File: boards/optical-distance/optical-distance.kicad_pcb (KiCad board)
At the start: 2 copper layers, 25 x 19.5 mm, 6 parts, among them J1 CONN_02X03, M2 MountingHole_2.2mm_M2, U1 DS9638

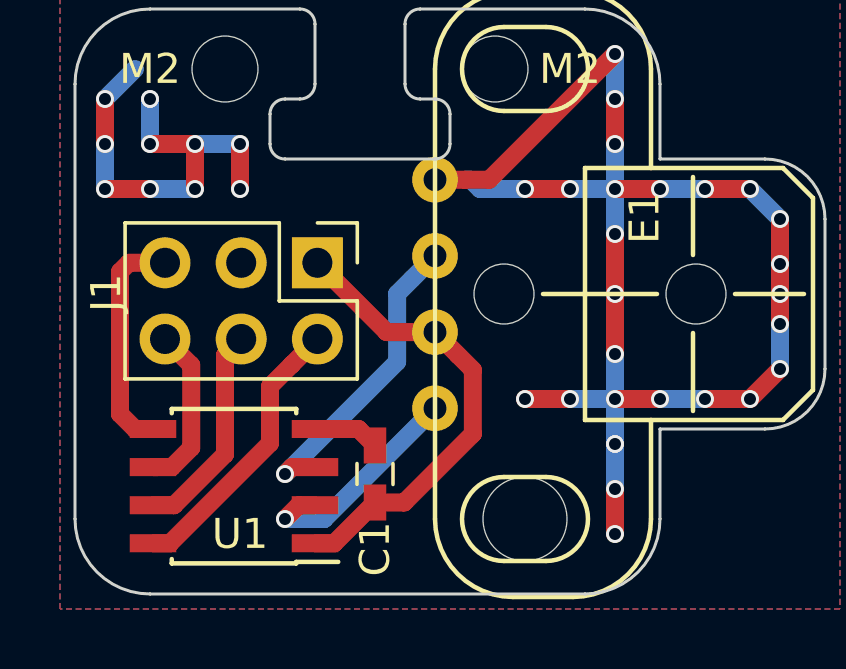
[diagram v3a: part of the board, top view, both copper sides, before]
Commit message: boards/op_v3: heat resistors in parallel added
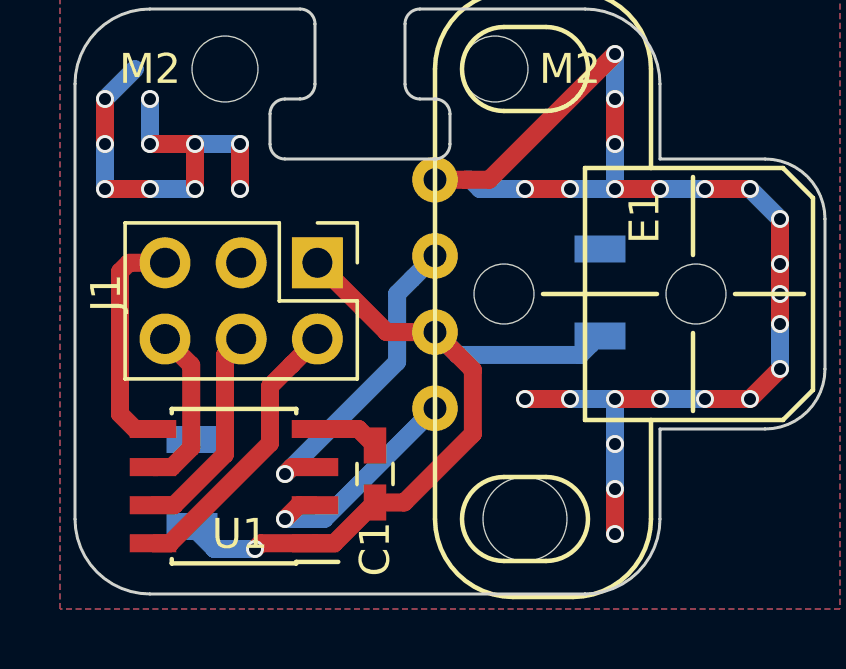
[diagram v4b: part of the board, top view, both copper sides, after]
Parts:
- added R1: HEAT, Resistors_SMD:R_1206, B.Cu at (102.5, 44.5)
- added R2: HEAT, Resistors_SMD:R_1206, B.Cu at (88.9, 50.8)
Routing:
- net /VCC: track 15.6 -> 26.1 mm, vias 0 -> 1
- net /GND: track 51.9 -> 44.9 mm, vias 26 -> 23
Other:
- board text added: "optical- distance"
- board text removed: "optical-dis- tance board"
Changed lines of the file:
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@@
-(kicad_pcb (version 4) (host pcbnew 4.0.6)
+(kicad_pcb (version 4) (host pcbnew 4.0.7-e2-6376~58~ubuntu16.04.1)
   (general
-    (links 12)
+    (links 16)
     (no_connects 1)
     (area 84.949999 34.949999 110.050001 54.550001)
     (thickness 1.6)
     (drawings 40)
-    (tracks 124)
+    (tracks 126)
     (zones 0)
-    (modules 6)
+    (modules 8)
     (nets 9)
   )
@@
     (39 F.Mask user)
     (40 Dwgs.User user)
-    (41 Cmts.User user)
+    (41 Cmts.User user hide)
     (42 Eco1.User user)
     (43 Eco2.User user)
@@
     (46 B.CrtYd user)
     (47 F.CrtYd user)
-    (48 B.Fab user)
-    (49 F.Fab user)
+    (48 B.Fab user hide)
+    (49 F.Fab user hide)
   )
   (setup
@@
     (mod_text_size 1 1)
     (mod_text_width 0.15)
-    (pad_size 1.5 1.5)
-    (pad_drill 0.6)
+    (pad_size 0.9 1.7)
+    (pad_drill 0)
     (pad_to_mask_clearance 0)
     (aux_axis_origin 0 0)
@@
     (pad 1 np_thru_hole circle (at 0 0) (size 2.2 2.2) (drill 2.2) (layers *.Cu *.Mask))
   )
+  (module Resistors_SMD:R_1206 (layer B.Cu)
+    (at 102.5 44.45 90)
+    (descr "Resistor SMD 1206, reflow soldering, Vishay (see dcrcw.pdf)")
+    (tags "resistor 1206")
+    (attr smd)
+    (fp_text reference R1 (at -0.05 0 90) (layer B.SilkS)
+      (effects (font (size 1 1) (thickness 0.15)) (justify mirror))
+    )
+    (fp_text value HEAT (at 0 -1.95 90) (layer B.Fab)
+      (effects (font (size 1 1) (thickness 0.15)) (justify mirror))
+    )
+    (fp_text user %R (at 0 0 90) (layer B.Fab)
+      (effects (font (size 0.7 0.7) (thickness 0.105)) (justify mirror))
+    )
+    (fp_line (start -1.6 -0.8) (end -1.6 0.8) (layer B.Fab) (width 0.1))
+    (fp_line (start 1.6 -0.8) (end -1.6 -0.8) (layer B.Fab) (width 0.1))
+    (fp_line (start 1.6 0.8) (end 1.6 -0.8) (layer B.Fab) (width 0.1))
+    (fp_line (start -1.6 0.8) (end 1.6 0.8) (layer B.Fab) (width 0.1))
+    (fp_line (start 1 -1.07) (end -1 -1.07) (layer B.SilkS) (width 0.12))
+    (fp_line (start -1 1.07) (end 1 1.07) (layer B.SilkS) (width 0.12))
+    (fp_line (start -2.15 1.11) (end 2.15 1.11) (layer B.CrtYd) (width 0.05))
+    (fp_line (start -2.15 1.11) (end -2.15 -1.1) (layer B.CrtYd) (width 0.05))
+    (fp_line (start 2.15 -1.1) (end 2.15 1.11) (layer B.CrtYd) (width 0.05))
+    (fp_line (start 2.15 -1.1) (end -2.15 -1.1) (layer B.CrtYd) (width 0.05))
+    (pad 1 smd rect (at -1.45 0 90) (size 0.9 1.7) (layers B.Cu B.Paste B.Mask)
+      (net 3 /VCC))
+    (pad 2 smd rect (at 1.45 0 90) (size 0.9 1.7) (layers B.Cu B.Paste B.Mask)
+      (net 4 /GND) (zone_connect 2))
+    (model ${KISYS3DMOD}/Resistors_SMD.3dshapes/R_1206.wrl
+      (at (xyz 0 0 0))
+      (scale (xyz 1 1 1))
+      (rotate (xyz 0 0 0))
+    )
+  )
+  (module Resistors_SMD:R_1206 (layer B.Cu)
+    (at 88.9 50.8 90)
+    (descr "Resistor SMD 1206, reflow soldering, Vishay (see dcrcw.pdf)")
+    (tags "resistor 1206")
+    (attr smd)
+    (fp_text reference R2 (at 0 0.1 90) (layer B.SilkS)
+      (effects (font (size 1 1) (thickness 0.15)) (justify mirror))
+    )
+    (fp_text value HEAT (at 0 -1.95 90) (layer B.Fab)
+      (effects (font (size 1 1) (thickness 0.15)) (justify mirror))
+    )
+    (fp_text user %R (at 0 0 90) (layer B.Fab)
+      (effects (font (size 0.7 0.7) (thickness 0.105)) (justify mirror))
+    )
+    (fp_line (start -1.6 -0.8) (end -1.6 0.8) (layer B.Fab) (width 0.1))
+    (fp_line (start 1.6 -0.8) (end -1.6 -0.8) (layer B.Fab) (width 0.1))
+    (fp_line (start 1.6 0.8) (end 1.6 -0.8) (layer B.Fab) (width 0.1))
+    (fp_line (start -1.6 0.8) (end 1.6 0.8) (layer B.Fab) (width 0.1))
+    (fp_line (start 1 -1.07) (end -1 -1.07) (layer B.SilkS) (width 0.12))
+    (fp_line (start -1 1.07) (end 1 1.07) (layer B.SilkS) (width 0.12))
+    (fp_line (start -2.15 1.11) (end 2.15 1.11) (layer B.CrtYd) (width 0.05))
+    (fp_line (start -2.15 1.11) (end -2.15 -1.1) (layer B.CrtYd) (width 0.05))
+    (fp_line (start 2.15 -1.1) (end 2.15 1.11) (layer B.CrtYd) (width 0.05))
+    (fp_line (start 2.15 -1.1) (end -2.15 -1.1) (layer B.CrtYd) (width 0.05))
+    (pad 1 smd rect (at -1.45 0 90) (size 0.9 1.7) (layers B.Cu B.Paste B.Mask)
+      (net 3 /VCC))
+    (pad 2 smd rect (at 1.45 0 90) (size 0.9 1.7) (layers B.Cu B.Paste B.Mask)
+      (net 4 /GND) (zone_connect 2))
+    (model ${KISYS3DMOD}/Resistors_SMD.3dshapes/R_1206.wrl
+      (at (xyz 0 0 0))
+      (scale (xyz 1 1 1))
+      (rotate (xyz 0 0 0))
+    )
+  )
   (gr_text rev3 (at 100.4 39.7) (layer B.SilkS)
     (effects (font (size 1.5 1.5) (thickness 0.3)) (justify mirror))
@@
     (effects (font (size 1 1) (thickness 0.2)) (justify mirror))
   )
-  (gr_text "optical-dis-\ntance board" (at 91.325 51.435) (layer B.SilkS)
+  (gr_text "optical-\ndistance" (at 94.5 52) (layer B.SilkS)
     (effects (font (size 1 1) (thickness 0.2)) (justify mirror))
   )
@@
     (effects (font (size 1.5 1.5) (thickness 0.3)) (justify mirror))
   )
-  (gr_text A* (at 90.5 48.5 270) (layer B.SilkS)
-    (effects (font (size 1.5 1.5) (thickness 0.3)) (justify mirror))
+  (gr_text A* (at 91 48 270) (layer B.SilkS)
+    (effects (font (size 1 1) (thickness 0.15)) (justify mirror))
   )
   (gr_text A (at 93 48 270) (layer B.SilkS)
@@
   (gr_line (start 92 40) (end 97 40) (layer Edge.Cuts) (width 0.1))
   (gr_text B* (at 88 41 270) (layer B.SilkS)
-    (effects (font (size 1.5 1.5) (thickness 0.3)) (justify mirror))
+    (effects (font (size 1 1) (thickness 0.15)) (justify mirror))
   )
   (gr_text GND (at 90.5 40.5 270) (layer B.SilkS)
-    (effects (font (size 1.5 1.2) (thickness 0.3)) (justify mirror))
+    (effects (font (size 1 1) (thickness 0.15)) (justify mirror))
   )
   (gr_text 5V (at 93 41.1 270) (layer B.SilkS)
-    (effects (font (size 1.5 1.1) (thickness 0.275)) (justify mirror))
+    (effects (font (size 1 1) (thickness 0.15)) (justify mirror))
   )
   (dimension 24 (width 0.3) (layer Dwgs.User)
@@
   (segment (start 92.46 51.54) (end 92 52) (width 0.6) (layer F.Cu) (net 2))
   (via (at 92 52) (size 0.6) (drill 0.4) (layers F.Cu B.Cu) (net 2))
+  (segment (start 91 53) (end 89.65 53) (width 0.6) (layer B.Cu) (net 3))
+  (segment (start 89.65 53) (end 88.9 52.25) (width 0.6) (layer B.Cu) (net 3))
+  (segment (start 93 52.81) (end 91.19 52.81) (width 0.6) (layer F.Cu) (net 3))
+  (segment (start 91.19 52.81) (end 91 53) (width 0.6) (layer F.Cu) (net 3))
+  (via (at 91 53) (size 0.6) (drill 0.4) (layers F.Cu B.Cu) (net 3))
+  (segment (start 97.761999 46.531999) (end 101.836617 46.531999) (width 0.6) (layer B.Cu) (net 3))
+  (segment (start 101.836617 46.531999) (end 102.19999 46.168626) (width 0.6) (layer B.Cu) (net 3))
+  (segment (start 102.19999 46.168626) (end 102.484308 45.884308) (width 0.6) (layer B.Cu) (net 3))
+  (segment (start 97 45.77) (end 97.761999 46.531999) (width 0.6) (layer B.Cu) (net 3))
   (segment (start 97 45.77) (end 95.39 45.77) (width 0.6) (layer F.Cu) (net 3))
   (segment (start 95.39 45.77) (end 93.08 43.46) (width 0.6) (layer F.Cu) (net 3))
@@
   (segment (start 93 52.81) (end 93.64 52.81) (width 0.6) (layer F.Cu) (net 3))
   (segment (start 93.64 52.81) (end 95 51.45) (width 0.6) (layer F.Cu) (net 3))
-  (segment (start 103 44.5) (end 103 46.5) (width 0.6) (layer F.Cu) (net 4))
-  (segment (start 103 42.5) (end 103 44.5) (width 0.6) (layer F.Cu) (net 4))
-  (via (at 103 44.5) (size 0.6) (drill 0.4) (layers F.Cu B.Cu) (net 4))
   (segment (start 101.5 48) (end 100 48) (width 0.6) (layer F.Cu) (net 4))
   (via (at 100 48) (size 0.6) (drill 0.4) (layers F.Cu B.Cu) (net 4))
@@
   (segment (start 103 41) (end 101.5 41) (width 0.6) (layer B.Cu) (net 4))
   (via (at 101.5 41) (size 0.6) (drill 0.4) (layers F.Cu B.Cu) (net 4))
-  (segment (start 103 46.5) (end 103 48) (width 0.6) (layer B.Cu) (net 4))
-  (via (at 103 46.5) (size 0.6) (drill 0.4) (layers F.Cu B.Cu) (net 4))
-  (segment (start 103 41) (end 103 42.5) (width 0.6) (layer B.Cu) (net 4))
-  (via (at 103 42.5) (size 0.6) (drill 0.4) (layers F.Cu B.Cu) (net 4))
   (segment (start 103 51) (end 103 52.5) (width 0.6) (layer F.Cu) (net 4))
   (via (at 103 52.5) (size 0.6) (drill 0.4) (layers F.Cu B.Cu) (net 4))

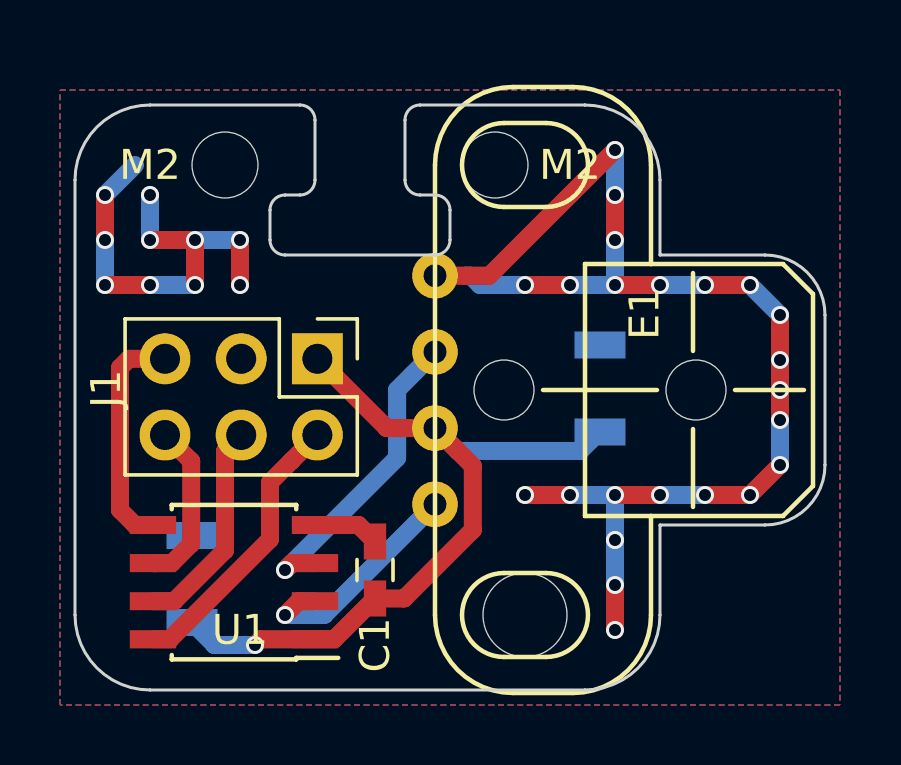
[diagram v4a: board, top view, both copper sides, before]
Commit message: boards/op_v3: spacing 10mm, from side 3mm, overall dimensions edited
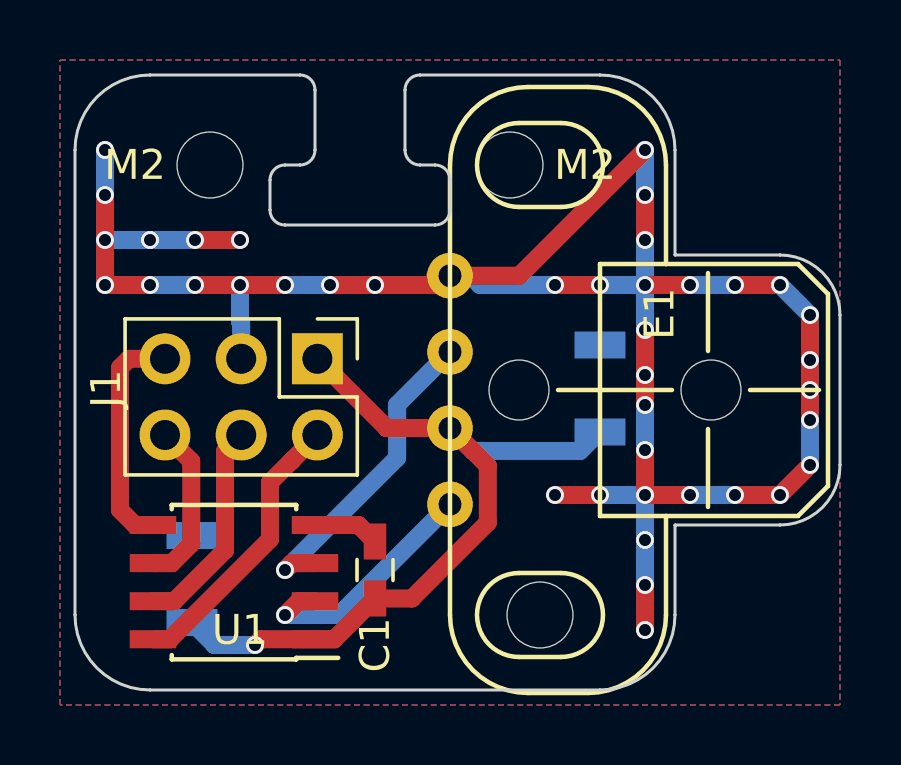
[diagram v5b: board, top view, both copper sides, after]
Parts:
- moved E1 0.50 mm to (97.5, 44.5)
- moved M2 0.50 mm to (99.5, 37.0)
- moved M2 0.50 mm to (89.5, 37.0)
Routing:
- net /GND: track 44.9 -> 77.5 mm, vias 23 -> 40
- net (no net): track 17.9 -> 0.00 mm, vias 10 -> 0
- net /VCC: track 26.1 -> 28.1 mm
- net Net-(E1-Pad4): track 7.72 -> 8.22 mm
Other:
- board size 25 x 19.5 mm -> 25.5 x 20.5 mm

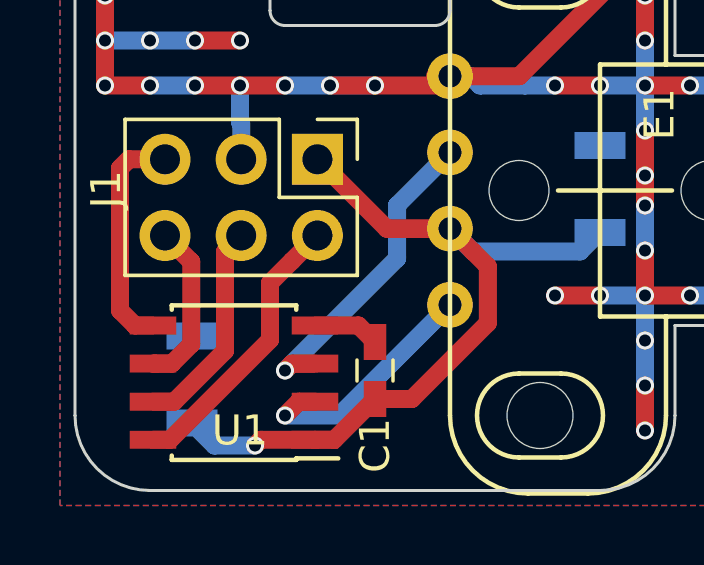
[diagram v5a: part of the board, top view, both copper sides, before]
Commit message: [optical distance] fix GND connection
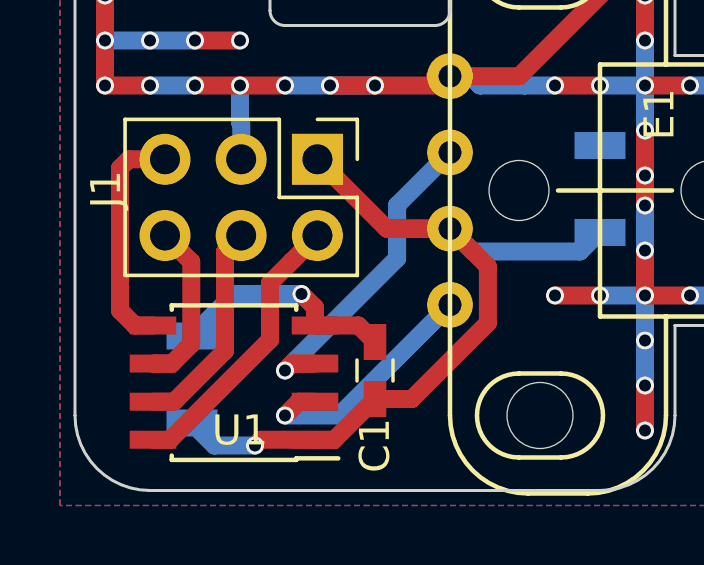
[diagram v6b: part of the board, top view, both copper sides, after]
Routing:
- net /GND: track 77.5 -> 83.0 mm, vias 40 -> 41
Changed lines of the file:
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@@
-(kicad_pcb (version 4) (host pcbnew 4.0.7-e2-6376~58~ubuntu16.04.1)
+(kicad_pcb (version 4) (host pcbnew 4.0.6)
   (general
     (links 16)
-    (no_connects 1)
-    (area 84.949999 33.949999 110.550001 54.550001)
+    (no_connects 0)
+    (area 53.525 33.5 122.057143 62.415001)
     (thickness 1.6)
     (drawings 40)
-    (tracks 143)
+    (tracks 148)
     (zones 0)
     (modules 8)
@@
     (visible_elements 7FFFFFFF)
     (pcbplotparams
-      (layerselection 0x00030_80000001)
-      (usegerberextensions false)
+      (layerselection 0x010f0_80000001)
+      (usegerberextensions true)
       (excludeedgelayer true)
       (linewidth 0.100000)
@@
       (outputformat 1)
       (mirror false)
-      (drillshape 1)
+      (drillshape 0)
       (scaleselection 1)
-      (outputdirectory ""))
+      (outputdirectory gerber/))
   )
   (net 0 "")
@@
   (segment (start 93 52.81) (end 93.64 52.81) (width 0.6) (layer F.Cu) (net 3))
   (segment (start 93.64 52.81) (end 95 51.45) (width 0.6) (layer F.Cu) (net 3))
+  (segment (start 92.55 47.95) (end 90.3 47.95) (width 0.6) (layer B.Cu) (net 4))
+  (segment (start 90.3 47.95) (end 88.9 49.35) (width 0.6) (layer B.Cu) (net 4))
+  (segment (start 93 49) (end 93 48.4) (width 0.6) (layer F.Cu) (net 4))
+  (via (at 92.55 47.95) (size 0.6) (drill 0.4) (layers F.Cu B.Cu) (net 4))
+  (segment (start 93 48.4) (end 92.55 47.95) (width 0.6) (layer F.Cu) (net 4))
   (segment (start 104 46.5) (end 104 48) (width 0.6) (layer F.Cu) (net 4))
   (segment (start 104 45) (end 104 46.5) (width 0.6) (layer B.Cu) (net 4))
